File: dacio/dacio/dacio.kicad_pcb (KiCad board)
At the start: 4 copper layers, 90.2 x 50 mm, 56 parts, among them J3 RJ45_Shielded, J4 RJ45_Shielded, J5 Conn_02x12_Odd_Even, U1 SN74LVC1T45DBV, U10 MAX3232, U11 MAX3232, U12 74HCT32D, U13 74HCT00D, U14 74HCT32D, U15 74HCT00D, U16 TLV70033_SOT353, U17 SN74LV8T374PWR, U18 SN74LV8T374PWR, U2 SN74LVC1T45DBV, U3 TLV70018_SOT353, U4 MAX487CSA+, U5 MAX487CSA+, U6 MAX487CSA+, U7 MAX487CSA+, U8 MAX487CSA+, U9 MAX487CSA+

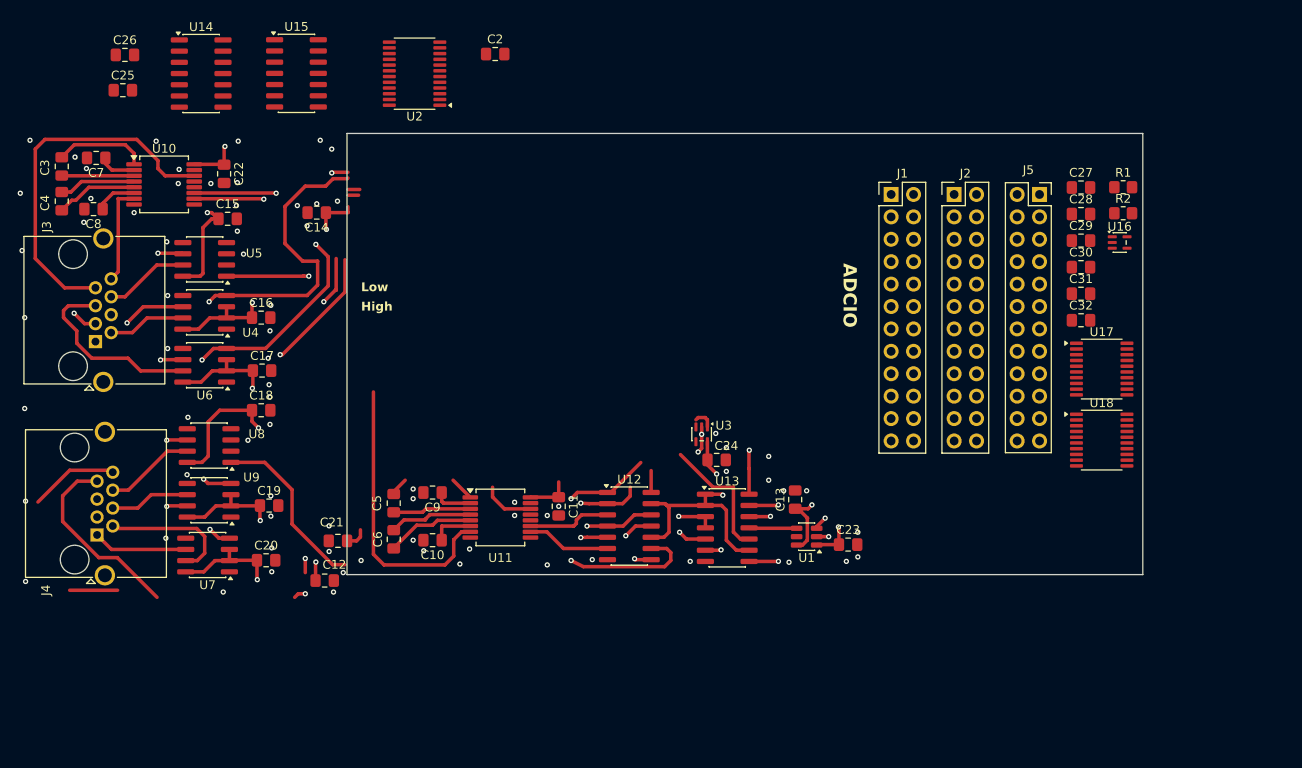
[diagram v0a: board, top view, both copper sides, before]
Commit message: Use the correct pin-headers.
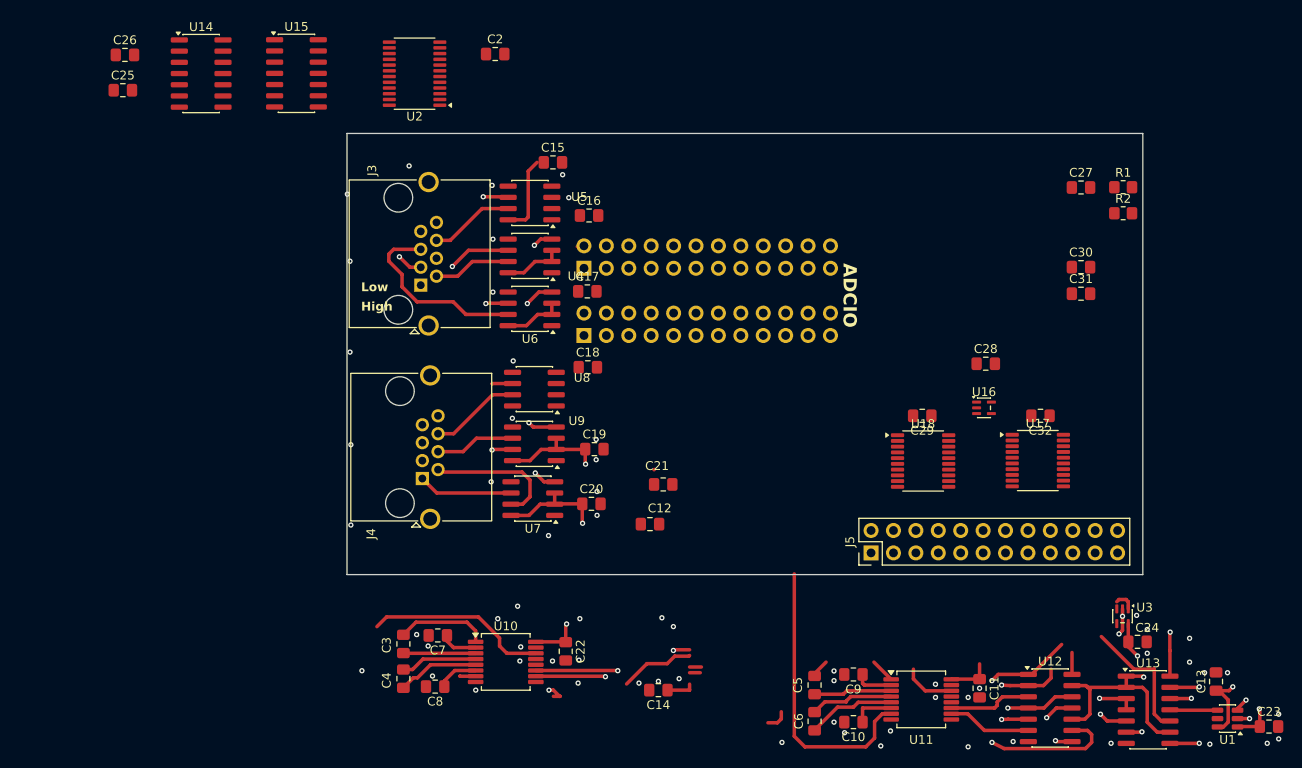
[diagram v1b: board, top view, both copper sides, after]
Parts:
- J1, J2: footprint Connector_PinHeader_2.54mm:PinHeader_2x12_P2.54mm_Vertical -> Connector_PinSocket_2.54mm:PinSocket_2x12_P2.54mm_Vertical; moved to B.Cu
- J5: footprint Connector_PinSocket_2.54mm:PinSocket_2x12_P2.54mm_Vertical -> Connector_PinHeader_2.54mm:PinHeader_2x12_P2.54mm_Vertical
- U17, U18: footprint Package_SO:TSSOP-20_4.4x6.5mm_P0.65mm -> Package_SO:Texas_PW0020A_TSSOP-20_4.4x6.5mm_P0.65mm
- moved C22 66.5 mm to (160.5, 137.4)
- moved C3 66.5 mm to (142.1, 136.6)
- moved C4 66.5 mm to (142.1, 140.5)
- moved C7 66.5 mm to (146.0, 135.6)
- moved C8 66.5 mm to (145.7, 141.4)
- moved U10 66.5 mm to (153.7, 138.6)
- moved C14 66.5 mm to (171.0, 141.8)
- moved C11 52.0 mm to (207.4, 141.6)
- moved C24 52.0 mm to (225.3, 136.3)
- moved U12 52.0 mm to (215.4, 143.8)
- moved C10 52.0 mm to (193.1, 145.4)
- moved C13 52.0 mm to (234.2, 140.8)
- moved C23 52.0 mm to (240.2, 145.9)
- moved C5 52.0 mm to (188.7, 141.2)
- moved C6 52.0 mm to (188.7, 145.3)
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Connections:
- J1 pad 11: Net-(J1-GND-Pad11) -> GND
- J1 pad 14: Net-(J1-GND-Pad11) -> GND
- J1 pad 17: Net-(J1-GND-Pad11) -> GND
- J1 pad 2: Net-(J1-GND-Pad11) -> GND
- J1 pad 20: Net-(J1-GND-Pad11) -> GND
- J1 pad 23: Net-(J1-GND-Pad11) -> GND
- J1 pad 5: Net-(J1-GND-Pad11) -> GND
- J1 pad 8: Net-(J1-GND-Pad11) -> GND
- J2 pad 10: Net-(J2-GND-Pad10) -> GND
- J2 pad 13: Net-(J2-GND-Pad10) -> GND
- J2 pad 15: Net-(J2-GND-Pad10) -> GND
- J2 pad 16: Net-(J2-GND-Pad10) -> GND
- J2 pad 17: Net-(J2-5v-Pad17) -> 5v
- J2 pad 18: Net-(J2-GND-Pad10) -> GND
- J2 pad 19: Net-(J2-5v-Pad17) -> 5v
- J2 pad 2: Net-(J2-GND-Pad10) -> GND
- J2 pad 20: Net-(J2-GND-Pad10) -> GND
- J2 pad 21: Net-(J2-GND-Pad10) -> GND
- J2 pad 23: Net-(J2-GND-Pad10) -> GND
- J2 pad 5: Net-(J2-GND-Pad10) -> GND
- J2 pad 7: Net-(J2-GND-Pad10) -> GND
- J2 pad 8: Net-(J2-GND-Pad10) -> GND
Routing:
- net Net-(U10-T1IN): track 66.4 -> 11.2 mm
- net Net-(U5-RO): track 57.0 -> 3.24 mm, vias 2 -> 1
- net Net-(U10-T2IN): track 63.1 -> 11.2 mm
- net SEL2: track 74.1 -> 24.0 mm
- net SEL1: track 56.3 -> 9.14 mm, vias 2 -> 1
- net SEL0: track 69.7 -> 25.9 mm, vias 4 -> 2
- net 5v: track 110.7 -> 82.7 mm, vias 11 -> 6
- net Net-(U8-A): track 31.5 -> 4.46 mm, vias 1 -> 0
- net SPI_CLK: track 25.8 -> 0.00 mm
- net SPI_OUT: track 24.3 -> 1.87 mm
- net CLK0: track 33.0 -> 10.7 mm
- net Net-(U11-T1OUT): track 27.7 -> 5.96 mm
- net Net-(U10-T1OUT): track 41.3 -> 20.7 mm
- net Net-(U8-RO): track 34.7 -> 14.7 mm
- net OUT0: track 23.1 -> 3.32 mm, vias 2 -> 1
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
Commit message: Fixed some of the layout.
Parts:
- moved C26 110.7 mm to (221.2, 74.2)
- moved C25 99.6 mm to (207.1, 97.5)
- moved U14 84.0 mm to (199.9, 95.0), turned to -90 degrees
- moved U15 80.3 mm to (209.1, 85.9)
- moved C23 74.8 mm to (214.1, 75.8)
- moved C14 69.8 mm to (188.7, 74.2)
- moved C11 62.4 mm to (187.2, 82.6)
- moved C9 62.4 mm to (172.8, 81.0)
- moved C5 62.4 mm to (168.4, 82.2)
- moved C6 62.4 mm to (168.4, 86.3)
- moved U11 62.4 mm to (180.5, 83.9)
- moved U12 62.4 mm to (195.2, 84.8)
- moved C10 62.4 mm to (172.8, 86.5)
- moved C12 61.6 mm to (207.7, 74.2)
- moved R1 60.7 mm to (162.9, 83.2), turned to 90 degrees
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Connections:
- J5 pad 10: GND -> LOW_ERR
- J5 pad 11: LOW_DIR0 -> LED_CLK
- J5 pad 12: HIGH_DIR0 -> LED_OUT
- J5 pad 13: LOW_DIR1 -> unconnected-(J5-Pin_13-Pad13)
- J5 pad 14: HIGH_DIR1 -> GND
- J5 pad 15: LOW_DIR2 -> GND
- J5 pad 16: HIGH_DIR2 -> HIGH_ERR
- J5 pad 17: GND -> HIGH_DIR1
- J5 pad 18: GND -> HIGH_DIR2
- J5 pad 19: LOW_ERR -> GND
- J5 pad 2: HIGH_LEV0 -> LOW_LEV1
- J5 pad 20: HIGH_ERR -> HIGH_DIR0
- J5 pad 21: LED_CLK -> HIGH_LEV2
- J5 pad 22: GND -> HIGH_LEV3
- J5 pad 23: LED_OUT -> HIGH_LEV0
- J5 pad 24: LED_CS -> HIGH_LEV1
- J5 pad 3: LOW_LEV1 -> LOW_LEV2
- J5 pad 4: HIGH_LEV1 -> LOW_LEV3
- J5 pad 5: LOW_LEV2 -> GND
- J5 pad 6: HIGH_LEV2 -> LOW_DIR0
- J5 pad 7: LOW_LEV3 -> LOW_DIR1
- J5 pad 8: HIGH_LEV3 -> LOW_DIR2
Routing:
- net HDR_LEV0: track 0.00 -> 100.7 mm, vias 0 -> 2
- net HDR_LEV1: track 0.00 -> 93.7 mm, vias 0 -> 2
- net HDR_LEV2: track 0.00 -> 81.1 mm, vias 0 -> 2
- net HDR_WR_HIGH: track 0.00 -> 80.9 mm, vias 0 -> 2
- net HDR_ERR: track 0.00 -> 71.3 mm, vias 0 -> 2
- net HDR_WR_LOW: track 0.00 -> 62.2 mm, vias 0 -> 2
- net Net-(U10-T2OUT): track 1.80 -> 63.9 mm, vias 0 -> 1
- net LED_OUT: track 0.00 -> 60.7 mm, vias 0 -> 1
- net LED_CLK: track 0.00 -> 57.2 mm, vias 0 -> 1
- net HDR_LEV3: track 0.00 -> 56.7 mm, vias 0 -> 3
- net Net-(U11-T1OUT): track 5.96 -> 60.3 mm, vias 0 -> 1
- net OUT0: track 3.32 -> 56.1 mm, vias 1 -> 4
- net Net-(U5-RO): track 3.24 -> 51.3 mm, vias 1 -> 4
- net Net-(U10-T1OUT): track 20.7 -> 67.6 mm, vias 0 -> 1
- net CLK1: track 2.61 -> 48.5 mm, vias 1 -> 2
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- added copper zone on In2.Cu, net 3.3v
- added copper zone on In2.Cu, net 5v
- added copper zone on B.Cu, net GND
- added copper zone on F.Cu, net GND

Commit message: Finalized layout for DACIO.
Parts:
- removed C14, C2, C21, C23: 100n, Capacitor_SMD:C_0805_2012Metric_Pad1.18x1.45mm_HandSolder
- moved C26 20.7 mm to (201.3, 80.1)
- moved C12 9.68 mm to (202.8, 82.6), turned to 180 degrees
- moved U15 1.08 mm to (209.8, 85.1), turned to 90 degrees
- moved J4 0.42 mm to (144.3, 95.8)
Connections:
- J5 pad 13: unconnected-(J5-Pin_13-Pad13) -> LED_CS
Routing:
- net Net-(U8-RO): track 0.97 -> 78.4 mm, vias 0 -> 3
- net SEL2: track 10.3 -> 83.1 mm, vias 0 -> 7
- net SPI_OUT: track 0.00 -> 72.1 mm, vias 0 -> 4
- net SEL0: track 9.61 -> 67.3 mm, vias 1 -> 4
- net Net-(U10-T2IN): track 0.00 -> 56.2 mm, vias 1 -> 2
- net SEL1: track 5.90 -> 61.3 mm, vias 1 -> 3
- net LED_CS: track 0.00 -> 54.1 mm
- net SPI_CLK: track 0.00 -> 50.5 mm, vias 0 -> 4
- net Net-(U10-T1IN): track 0.00 -> 50.1 mm, vias 0 -> 2
- net INV_SEL2: track 10.3 -> 56.5 mm, vias 2 -> 7
- net Net-(U14-Pad10): track 0.00 -> 44.4 mm
- net Net-(U14-Pad2): track 0.00 -> 33.0 mm
- net Net-(U9-B): track 20.9 -> 36.3 mm
- net Net-(U15-Pad12): track 0.00 -> 10.4 mm
- net 5v: track 116.8 -> 123.9 mm, vias 15 -> 16
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- added copper zone on In1.Cu, net 5v
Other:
- board size 90.2 x 50 mm -> 90.2 x 50.4 mm
- board text added: "DAC IO"
- board text removed: "ADCIO"

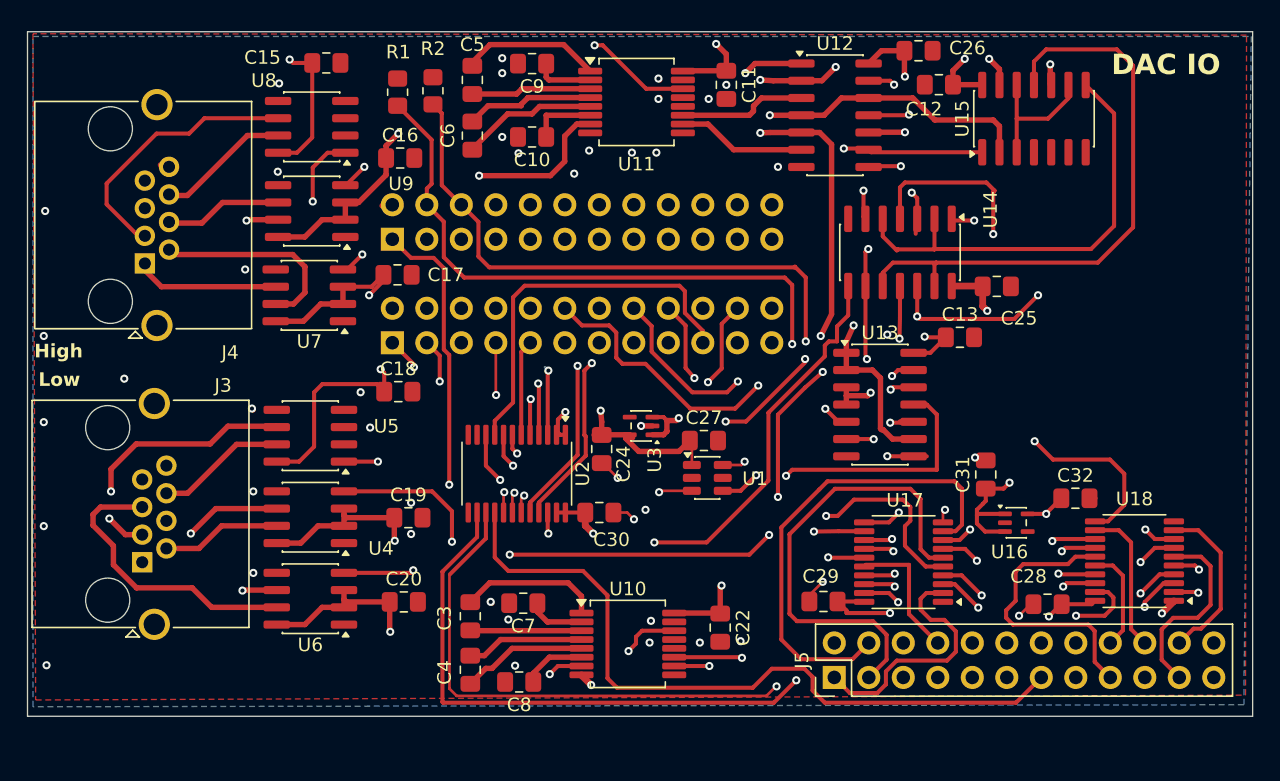
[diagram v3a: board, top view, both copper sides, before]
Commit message: Changed debug-header to data & address bus
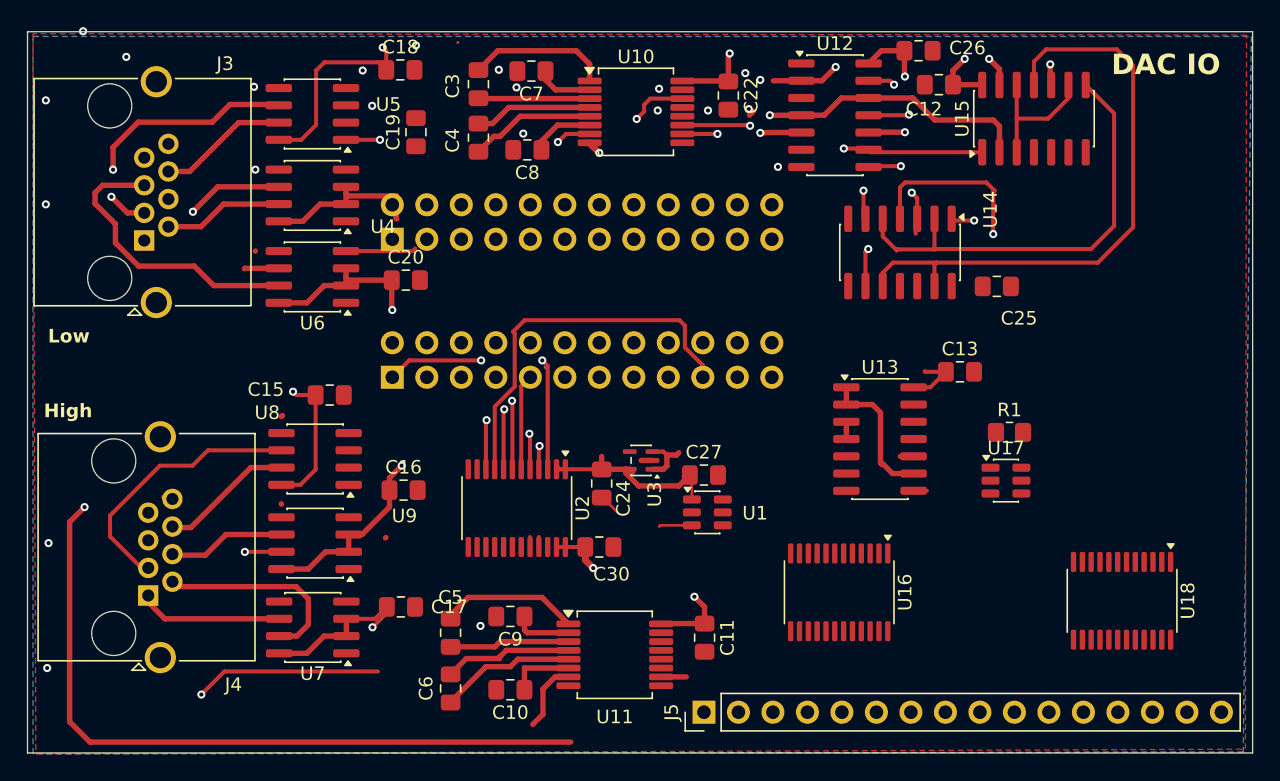
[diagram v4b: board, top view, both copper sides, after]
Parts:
- removed C28, C29, C31, C32: 100n, Capacitor_SMD:C_0805_2012Metric_Pad1.18x1.45mm_HandSolder
- removed R2: 10k, Resistor_SMD:R_0805_2012Metric_Pad1.20x1.40mm_HandSolder
- J5: value Conn_02x12_Odd_Even -> Conn_01x16_Socket; footprint Connector_PinHeader_2.54mm:PinHeader_2x12_P2.54mm_Vertical -> Connector_PinHeader_2.54mm:PinHeader_1x16_P2.54mm_Vertical
- U16: value TLV70033_SOT353 -> SN74LVC1T45DBV; footprint Package_TO_SOT_SMD:SOT-353_SC-70-5 -> Package_SO:TSSOP-24_4.4x7.8mm_P0.65mm
- U17: value SN74LV8T374PWR -> SN74LVC1T45DBV; footprint Package_SO:Texas_PW0020A_TSSOP-20_4.4x6.5mm_P0.65mm -> Package_TO_SOT_SMD:SOT-23-6
- U18: value SN74LV8T374PWR -> SN74LVC1T45DBV; footprint Package_SO:Texas_PW0020A_TSSOP-20_4.4x6.5mm_P0.65mm -> Package_SO:TSSOP-24_4.4x7.8mm_P0.65mm
- moved R1 51.5 mm to (208.0, 108.2), turned to 0 degrees
- moved C10 40.7 mm to (171.2, 127.2)
- moved C11 40.7 mm to (185.6, 123.3)
- moved C5 40.7 mm to (166.8, 123.0)
- moved C6 40.7 mm to (166.8, 127.0)
- moved C9 40.7 mm to (171.2, 121.8)
- moved U11 40.7 mm to (178.9, 124.6)
- moved C7 39.2 mm to (172.8, 81.6)
- moved U10 39.2 mm to (180.5, 84.6)
- moved C22 39.2 mm to (187.3, 83.4)
- moved C3 39.2 mm to (168.9, 82.6)
- moved C4 39.2 mm to (168.9, 86.5)
- moved C8 39.2 mm to (172.5, 87.4)
- moved C19 28.4 mm to (164.3, 86.1), turned to 90 degrees
- moved C15 24.5 mm to (157.9, 105.5)
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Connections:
- J1 pad 10: HDR_LEV2 -> HDR_D2
- J1 pad 12: HDR_LEV3 -> HDR_D3
- J1 pad 15: HDR_LED_CS -> HDR_A0
- J1 pad 16: HDR_DIR0 -> HDR_D4
- J1 pad 18: HDR_DIR1 -> HDR_D5
- J1 pad 19: HDR_LED_CLK -> unconnected-(J1-DAC_06-Pad19)
- J1 pad 21: HDR_LED_OUT -> unconnected-(J1-DAC_07-Pad21)
- J1 pad 22: HDR_DIR2 -> HDR_D6
- J1 pad 24: HDR_ERR -> HDR_D7
- J1 pad 4: HDR_LEV0 -> HDR_D0
- J1 pad 6: HDR_LEV1 -> HDR_D1
- J2 pad 3: unconnected-(J2-DAC_09-Pad3) -> HDR_A3
- J2 pad 4: HDR_WR_LOW -> HDR_BAND
- J2 pad 6: HDR_WR_HIGH -> HDR_WR
- J5 pad 1: LOW_LEV0 -> GND
- J5 pad 10: LOW_ERR -> EXT_WR
- J5 pad 11: LED_CLK -> A0
- J5 pad 12: LED_OUT -> A1
- J5 pad 13: LED_CS -> A2
- J5 pad 14: GND -> A3
- J5 pad 15: GND -> BAND
- J5 pad 16: HIGH_ERR -> WR
- J5 pad 2: LOW_LEV1 -> D0
- J5 pad 3: LOW_LEV2 -> D1
- J5 pad 4: LOW_LEV3 -> D2
- J5 pad 5: GND -> D3
- J5 pad 6: LOW_DIR0 -> D4
- J5 pad 7: LOW_DIR1 -> D5
- J5 pad 8: LOW_DIR2 -> D6
- J5 pad 9: GND -> D7
- R1 pad 1: HDR_WR_LOW -> 5v
- R1 pad 2: GND -> EXT_WR
- U15 pad 4: GND -> HDR_EXT_WR
- U15 pad 5: GND -> HDR_EXT_WR
- U15 pad 6: unconnected-(U15-Pad6) -> Net-(U16-~{OE})
- U16 pad 1: 5v -> 1.8v
- U16 pad 2: GND -> HDR_EXT_WR
- U16 pad 3: 5v -> HDR_D7
- U16 pad 4: unconnected-(U16-NC-Pad4) -> HDR_D6
- U16 pad 5: 3.3v -> HDR_D5
- U17 pad 1: GND -> 1.8v
- U17 pad 2: LOW_LEV0 -> GND
- U17 pad 3: HDR_LEV0 -> HDR_EXT_WR
- U17 pad 4: HDR_LEV1 -> EXT_WR
- U17 pad 5: LOW_LEV1 -> GND
- U17 pad 6: LOW_LEV2 -> 5v
- U18 pad 1: GND -> 1.8v
- U18 pad 11: HDR_WR_HIGH -> GND
- U18 pad 12: HIGH_DIR0 -> GND
- U18 pad 13: HDR_DIR0 -> GND
- U18 pad 14: HDR_DIR1 -> unconnected-(U18-B8-Pad14)
- U18 pad 15: HIGH_DIR1 -> unconnected-(U18-B7-Pad15)
- U18 pad 16: HIGH_DIR2 -> A0
- U18 pad 17: HDR_DIR2 -> A1
- U18 pad 18: HDR_ERR -> A2
- U18 pad 19: HIGH_ERR -> A3
- U18 pad 2: HIGH_LEV0 -> 1.8v
- U18 pad 20: 3.3v -> BAND
- U18 pad 3: HDR_LEV0 -> HDR_WR
- U18 pad 4: HDR_LEV1 -> HDR_BAND
- U18 pad 5: HIGH_LEV1 -> HDR_A3
- U18 pad 6: HIGH_LEV2 -> HDR_A2
- U18 pad 7: HDR_LEV2 -> HDR_A1
- U18 pad 8: HDR_LEV3 -> HDR_A0
- U18 pad 9: HIGH_LEV3 -> GND
- U2 pad 10: HDR_LED_OUT -> GND
- U2 pad 14: LED_OUT -> unconnected-(U2-B8-Pad14)
- U2 pad 15: LED_CLK -> unconnected-(U2-B7-Pad15)
- U2 pad 16: LED_CS -> unconnected-(U2-B6-Pad16)
- U2 pad 8: HDR_LED_CS -> GND
- U2 pad 9: HDR_LED_CLK -> GND
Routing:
- net HDR_LEV0: track 100.7 -> 0.00 mm, vias 2 -> 0
- net HDR_LEV1: track 93.6 -> 0.00 mm, vias 2 -> 0
- net HDR_LEV2: track 82.3 -> 0.00 mm, vias 2 -> 0
- net HDR_WR_HIGH: track 80.8 -> 0.00 mm, vias 2 -> 0
- net Net-(U8-RO): track 78.4 -> 1.07 mm, vias 3 -> 0
- net HDR_ERR: track 72.0 -> 0.00 mm, vias 2 -> 0
- net Net-(U10-T1OUT): track 67.6 -> 4.28 mm
- net HDR_WR_LOW: track 63.1 -> 0.00 mm, vias 2 -> 0
- net GND: track 14.9 -> 76.6 mm, vias 44 -> 21
- net Net-(U10-T2OUT): track 63.9 -> 2.59 mm
- net LED_OUT: track 60.7 -> 0.00 mm, vias 1 -> 0
- net LED_CLK: track 56.8 -> 0.00 mm, vias 1 -> 0
- net HDR_LEV3: track 56.7 -> 0.00 mm, vias 3 -> 0
- net CLK0: track 55.0 -> 0.00 mm, vias 2 -> 0
- net LED_CS: track 54.1 -> 0.00 mm
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- removed copper zone on In2.Cu, net 3.3v
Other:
- board size 90.2 x 50.4 mm -> 90.2 x 53.1 mm

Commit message: fixed new layout
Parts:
- removed R1: 10k, Resistor_SMD:R_0805_2012Metric_Pad1.20x1.40mm_HandSolder
- removed U17: SN74LVC1T45DBV, Package_TO_SOT_SMD:SOT-23-6
- added C28: 100n, Capacitor_SMD:C_0805_2012Metric_Pad1.18x1.45mm_HandSolder, F.Cu at (201.7, 118.9)
- added C29: 100n, Capacitor_SMD:C_0805_2012Metric_Pad1.18x1.45mm_HandSolder, F.Cu at (222.3, 119.1)
- added C31: 100n, Capacitor_SMD:C_0805_2012Metric_Pad1.18x1.45mm_HandSolder, F.Cu at (201.4, 124.5)
- added C32: 100n, Capacitor_SMD:C_0805_2012Metric_Pad1.18x1.45mm_HandSolder, F.Cu at (222.4, 124.9)
- moved U13 9.75 mm to (208.0, 106.5)
- moved C13 9.75 mm to (213.8, 101.5)
- moved U16 1.96 mm to (194.9, 121.9)
- moved U18 1.43 mm to (216.0, 122.0)
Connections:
- J1 pad 19: unconnected-(J1-DAC_06-Pad19) -> HDR_A1
- J1 pad 21: unconnected-(J1-DAC_07-Pad21) -> HDR_A2
- J5 pad 10: EXT_WR -> GND
- U15 pad 4: HDR_EXT_WR -> GND
- U15 pad 5: HDR_EXT_WR -> GND
- U15 pad 6: Net-(U16-~{OE}) -> unconnected-(U15-Pad6)
- U16 pad 2: HDR_EXT_WR -> 1.8v
- U16 pad 22: Net-(U16-~{OE}) -> GND
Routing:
- net OUT1: track 2.23 -> 105.7 mm, vias 1 -> 2
- net Net-(U11-T1IN): track 0.00 -> 73.3 mm, vias 0 -> 3
- net CLK1: track 4.15 -> 76.7 mm, vias 1 -> 2
- net HDR_BAND: track 0.00 -> 70.9 mm
- net HDR_WR: track 0.00 -> 69.8 mm
- net Net-(U11-T2IN): track 1.85 -> 71.2 mm, vias 0 -> 3
- net HDR_A3: track 0.00 -> 67.9 mm
- net GND: track 76.6 -> 16.6 mm, vias 21 -> 106
- net HDR_D1: track 0.00 -> 58.7 mm, vias 0 -> 1
- net SEL0: track 50.9 -> 109.5 mm, vias 2 -> 3
- net Net-(U5-RO): track 3.09 -> 60.5 mm, vias 1 -> 3
- net SPI_CLK: track 13.7 -> 70.8 mm
- net Net-(U8-RO): track 1.07 -> 57.2 mm, vias 0 -> 2
- net HDR_D0: track 0.00 -> 54.6 mm
- net SEL2: track 54.7 -> 106.9 mm, vias 3 -> 6
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- added copper zone on In2.Cu, net 1.8v
